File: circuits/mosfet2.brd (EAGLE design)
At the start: 75.9 x 50.2 mm, 24 parts, among them IC2 IR4427S, J1 Power In 12V, J2 BED 24V, J3 Head 12V, J4 PSU GND, Q1 AOT240L, Q2 AOT240L

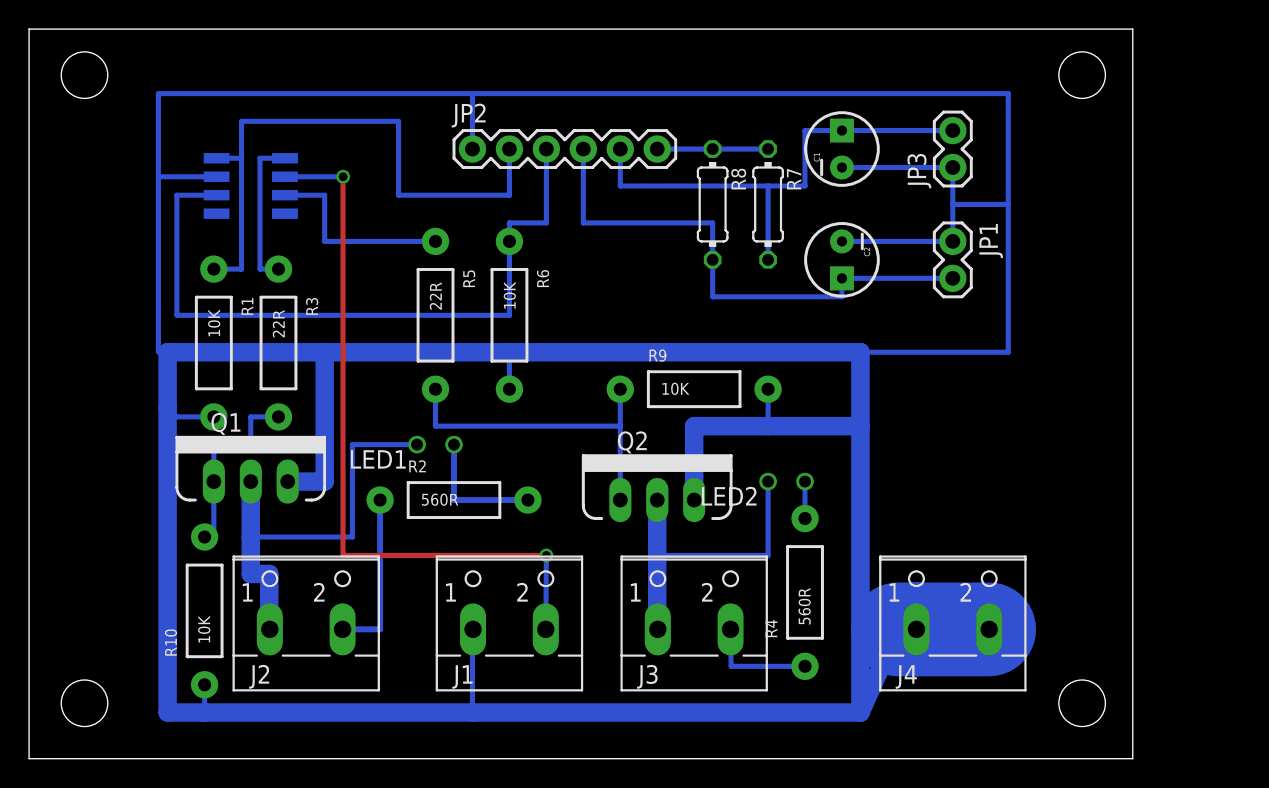
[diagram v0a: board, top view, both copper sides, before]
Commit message: update mosfet circuit
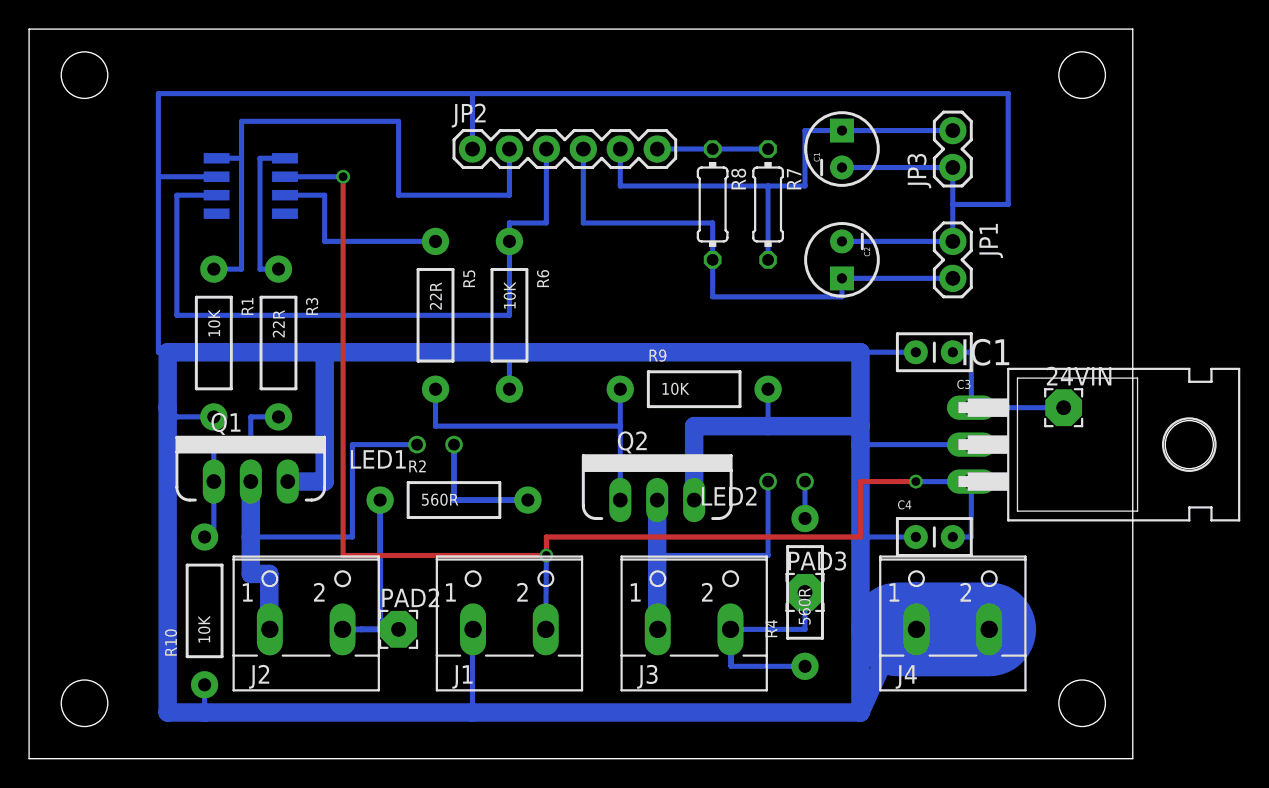
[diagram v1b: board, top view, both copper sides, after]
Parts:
- added 24VIN, PAD2, PAD3: WIREPAD2,54/1,0, wirepad:2,54/1,0
- added C3, C4: (no value), SparkFun-Passives:CAP-PTH-SMALLEZ
- added IC1: 7812T, adafruit:TO220H
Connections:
- new net N$1: 24VIN.1, C3.1, IC1.1
- net BEDV+: now also PAD2.1
- net GND: now also C3.2, C4.1, IC1.2
- net HEADV+: now also PAD3.1
- net VSS: now also C4.2, IC1.3
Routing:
- net GND: track 337.5 -> 380.7 mm
- net VSS: track 49.1 -> 88.5 mm, vias 2 -> 3
- net N$1: track 0.00 -> 11.4 mm
- net HEADV+: track 7.62 -> 17.8 mm
- net BEDV+: track 11.5 -> 14.0 mm
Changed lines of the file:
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@@
 <layer number="106" name="bPlate" color="7" fill="1" visible="yes" active="yes"/>
 <layer number="107" name="Crop" color="7" fill="1" visible="yes" active="yes"/>
+<layer number="108" name="fp8" color="7" fill="1" visible="no" active="yes"/>
+<layer number="109" name="fp9" color="7" fill="1" visible="no" active="yes"/>
+<layer number="110" name="fp0" color="7" fill="1" visible="no" active="yes"/>
+<layer number="111" name="LPC17xx" color="7" fill="1" visible="yes" active="yes"/>
+<layer number="112" name="tSilk" color="7" fill="1" visible="yes" active="yes"/>
 <layer number="116" name="Patch_BOT" color="9" fill="4" visible="yes" active="yes"/>
 <layer number="121" name="_tsilk" color="7" fill="1" visible="yes" active="yes"/>
 <layer number="122" name="_bsilk" color="7" fill="1" visible="yes" active="yes"/>
+<layer number="123" name="tTestmark" color="7" fill="1" visible="no" active="yes"/>
+<layer number="124" name="bTestmark" color="7" fill="1" visible="no" active="yes"/>
 <layer number="125" name="_tNames" color="7" fill="1" visible="yes" active="yes"/>
+<layer number="126" name="_bNames" color="7" fill="1" visible="yes" active="yes"/>
+<layer number="127" name="_tValues" color="7" fill="1" visible="yes" active="yes"/>
+<layer number="128" name="_bValues" color="7" fill="1" visible="yes" active="yes"/>
+<layer number="131" name="tAdjust" color="7" fill="1" visible="no" active="yes"/>
+<layer number="132" name="bAdjust" color="7" fill="1" visible="no" active="yes"/>
 <layer number="144" name="Drill_legend" color="7" fill="1" visible="yes" active="yes"/>
 <layer number="151" name="HeatSink" color="7" fill="1" visible="yes" active="yes"/>
+<layer number="152" name="_bDocu" color="7" fill="1" visible="yes" active="yes"/>
 <layer number="199" name="Contour" color="7" fill="1" visible="yes" active="yes"/>
 <layer number="200" name="200bmp" color="1" fill="10" visible="yes" active="yes"/>
@@
 <layer number="223" name="223bmp" color="24" fill="1" visible="no" active="no"/>
 <layer number="224" name="224bmp" color="25" fill="1" visible="no" active="no"/>
+<layer number="248" name="Housing" color="7" fill="1" visible="yes" active="yes"/>
+<layer number="249" name="Edge" color="7" fill="1" visible="yes" active="yes"/>
 <layer number="250" name="Descript" color="3" fill="1" visible="no" active="no"/>
 <layer number="251" name="SMDround" color="12" fill="11" visible="no" active="no"/>
@@
 <element name="R9" library="SparkFun-Resistors" package="AXIAL-0.4" value="10K" x="45.72" y="25.4"/>
 <element name="R10" library="SparkFun-Resistors" package="AXIAL-0.4" value="10K" x="12.065" y="10.16" rot="R90"/>
+<element name="IC1" library="adafruit" package="TO220H" value="7812T" x="74.93" y="21.59" rot="R270"/>
+<element name="24VIN" library="wirepad" package="2,54/1,0" value="WIREPAD2,54/1,0" x="71.12" y="24.13"/>
+<element name="PAD2" library="wirepad" package="2,54/1,0" value="WIREPAD2,54/1,0" x="25.4" y="8.89"/>
+<element name="PAD3" library="wirepad" package="2,54/1,0" value="WIREPAD2,54/1,0" x="53.34" y="11.43"/>
+<element name="C3" library="SparkFun-Passives" package="CAP-PTH-SMALLEZ" value="" x="63.5" y="27.94" rot="R180"/>
+<element name="C4" library="SparkFun-Passives" package="CAP-PTH-SMALLEZ" value="" x="60.96" y="15.24"/>
 </elements>
 <signals>
@@
 <wire x1="57.15" y1="27.94" x2="33.02" y2="27.94" width="1.27" layer="16"/>
 <wire x1="57.15" y1="27.94" x2="57.15" y2="22.86" width="1.27" layer="16"/>
-<wire x1="57.15" y1="22.86" x2="57.15" y2="3.175" width="1.27" layer="16"/>
+<wire x1="57.15" y1="22.86" x2="57.15" y2="21.59" width="1.27" layer="16"/>
+<wire x1="57.15" y1="21.59" x2="57.15" y2="15.24" width="1.27" layer="16"/>
+<wire x1="57.15" y1="15.24" x2="57.15" y2="3.175" width="1.27" layer="16"/>
 <wire x1="57.15" y1="3.175" x2="30.48" y2="3.175" width="1.27" layer="16"/>
 <contactref element="J4" pad="2"/>
@@
 <wire x1="50.8" y1="22.86" x2="57.15" y2="22.86" width="1.27" layer="16"/>
 <wire x1="67.31" y1="45.72" x2="67.31" y2="38.1" width="0.35" layer="16"/>
-<wire x1="67.31" y1="38.1" x2="67.31" y2="27.94" width="0.35" layer="16"/>
-<wire x1="67.31" y1="27.94" x2="57.15" y2="27.94" width="0.35" layer="16"/>
 <wire x1="63.5" y1="40.64" x2="63.5" y2="38.1" width="0.35" layer="16"/>
 <wire x1="63.5" y1="35.56" x2="63.5" y2="38.1" width="0.35" layer="16"/>
@@
 <wire x1="12.065" y1="5.08" x2="12.065" y2="3.175" width="0.35" layer="16"/>
 <wire x1="50.8" y1="25.4" x2="50.8" y2="22.86" width="0.35" layer="16"/>
+<wire x1="57.15" y1="27.94" x2="8.89" y2="27.94" width="0.35" layer="16"/>
+<contactref element="IC1" pad="2"/>
+<wire x1="64.77" y1="21.59" x2="57.15" y2="21.59" width="0.35" layer="16"/>
+<contactref element="C3" pad="2"/>
+<contactref element="C4" pad="1"/>
+<wire x1="60.96" y1="27.94" x2="57.15" y2="27.94" width="0.35" layer="16"/>
+<wire x1="60.96" y1="15.24" x2="57.15" y2="15.24" width="0.35" layer="16"/>
 </signal>
 <signal name="N$2">
@@
 <contactref element="R2" pad="P$1"/>
 <contactref element="J2" pad="2"/>
-<wire x1="21.55" y1="8.89" x2="24.13" y2="8.89" width="0.4064" layer="16"/>
+<wire x1="21.55" y1="8.89" x2="22.86" y2="8.89" width="0.4064" layer="16"/>
+<wire x1="22.86" y1="8.89" x2="24.13" y2="8.89" width="0.4064" layer="16"/>
 <wire x1="24.13" y1="8.89" x2="24.13" y2="17.78" width="0.4064" layer="16"/>
+<contactref element="PAD2" pad="1"/>
+<wire x1="25.4" y1="8.89" x2="22.86" y2="8.89" width="0.35" layer="16"/>
 </signal>
 <signal name="VSS">
@@
 <via x="21.59" y="40.005" extent="1-16" drill="0.6" shape="square"/>
 <wire x1="21.59" y1="40.005" x2="17.59" y2="40.005" width="0.35" layer="16"/>
+<contactref element="IC1" pad="3"/>
+<wire x1="64.77" y1="19.05" x2="60.96" y2="19.05" width="0.35" layer="16"/>
+<via x="60.96" y="19.05" extent="1-16" drill="0.6" shape="square"/>
+<wire x1="60.96" y1="19.05" x2="57.15" y2="19.05" width="0.35" layer="1"/>
+<wire x1="57.15" y1="19.05" x2="57.15" y2="15.24" width="0.35" layer="1"/>
+<wire x1="57.15" y1="15.24" x2="35.56" y2="15.24" width="0.35" layer="1"/>
+<wire x1="35.56" y1="15.24" x2="35.56" y2="13.97" width="0.35" layer="1"/>
+<contactref element="C4" pad="2"/>
+<wire x1="63.5" y1="15.24" x2="64.77" y2="15.24" width="0.35" layer="16"/>
+<wire x1="64.77" y1="15.24" x2="64.77" y2="19.05" width="0.35" layer="16"/>
 </signal>
 <signal name="N$5">
@@
 <wire x1="48.22" y1="8.89" x2="48.26" y2="6.35" width="0.35" layer="16"/>
 <wire x1="48.26" y1="6.35" x2="53.34" y2="6.35" width="0.35" layer="16"/>
+<contactref element="PAD3" pad="1"/>
+<wire x1="48.26" y1="6.35" x2="48.26" y2="8.89" width="0.35" layer="16"/>
+<wire x1="48.26" y1="8.89" x2="53.34" y2="8.89" width="0.35" layer="16"/>
+<wire x1="53.34" y1="8.89" x2="53.34" y2="11.43" width="0.35" layer="16"/>
 </signal>
 <signal name="BEDCTL">
@@
 <wire x1="46.99" y1="31.75" x2="46.99" y2="34.29" width="0.35" layer="16"/>
 </signal>
+<signal name="N$1">
+<contactref element="IC1" pad="1"/>
+<contactref element="24VIN" pad="1"/>
+<wire x1="64.77" y1="24.13" x2="71.12" y2="24.13" width="0.35" layer="16"/>
+<contactref element="C3" pad="1"/>
+<wire x1="63.5" y1="27.94" x2="64.77" y2="27.94" width="0.35" layer="16"/>
+<wire x1="64.77" y1="27.94" x2="64.77" y2="24.13" width="0.35" layer="16"/>
+</signal>
 </signals>
